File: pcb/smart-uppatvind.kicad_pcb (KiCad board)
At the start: 4 copper layers, 74 x 36 mm, 67 parts, among them J1 PWR, J2 QWIIC, J3 UART_PROG, J4 FAN, Q1 IRLML9301, Q2 MMBT3904, Q3 MMBT3904, Q4 MMBT3904, Q5 Q_NMOS_GSD, SW1 EN, SW2 MAIN, SW3 BOOT, SW4 FILTER, U1 LDL1117S33R, U2 L7980A, U3 ESP32-C3-WROOM-02, U4 M24C02-WMN

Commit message: Added testpoints
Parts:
- added TP1: VIN, TestPoint:TestPoint_THTPad_1.0x1.0mm_Drill0.5mm, F.Cu at (59.8, 75.1)
- added TP2: +5V, TestPoint:TestPoint_THTPad_1.0x1.0mm_Drill0.5mm, F.Cu at (124.6, 74.1)
- added TP3: VDD, TestPoint:TestPoint_THTPad_1.0x1.0mm_Drill0.5mm, F.Cu at (124.6, 70.7)
- added TP4: LED, TestPoint:TestPoint_Pad_1.0x1.0mm, B.Cu at (57.8, 58.3)
- added TP5: FAN_EN, TestPoint:TestPoint_Pad_1.0x1.0mm, B.Cu at (83.0, 53.5)
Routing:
- net /FAN_EN: track 10.8 -> 14.4 mm, vias 0 -> 1
- net /LED: track 29.2 -> 32.2 mm

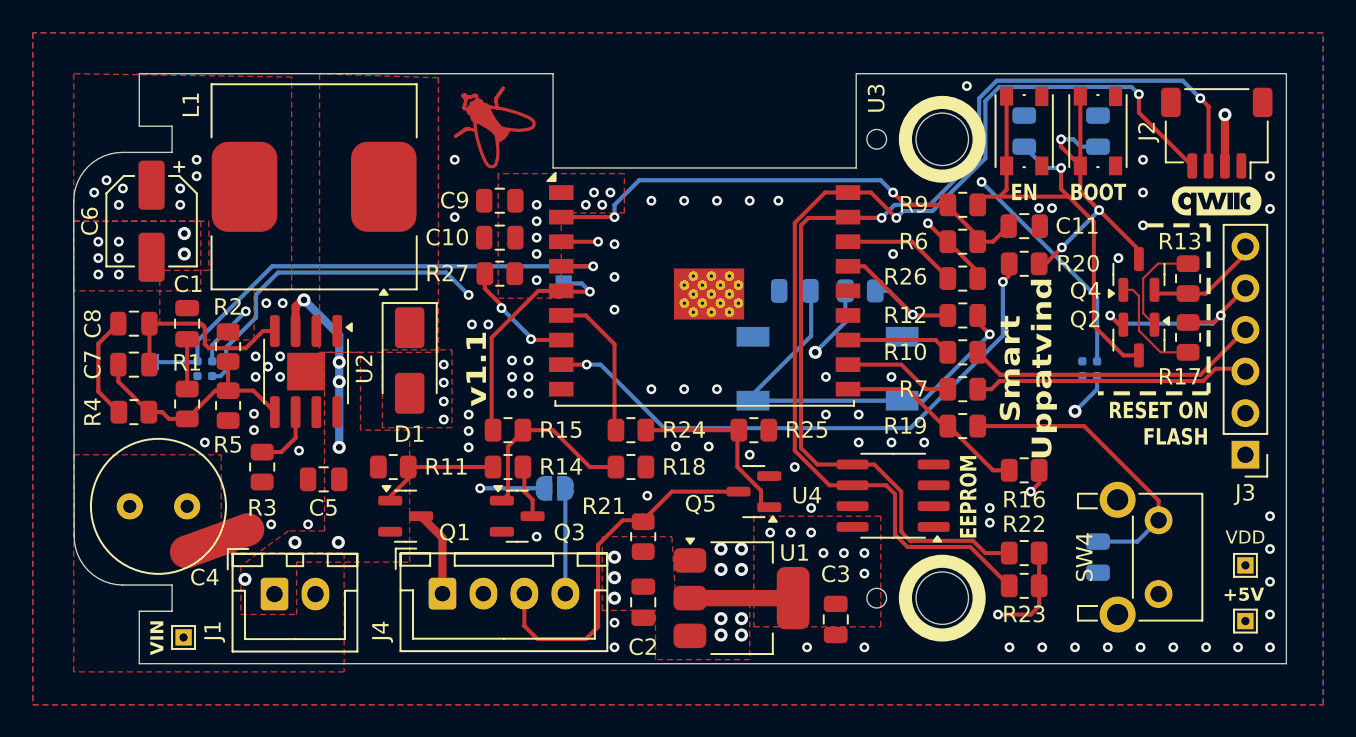
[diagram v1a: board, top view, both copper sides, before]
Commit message: Reannotated components geographically, adjusted designator positions
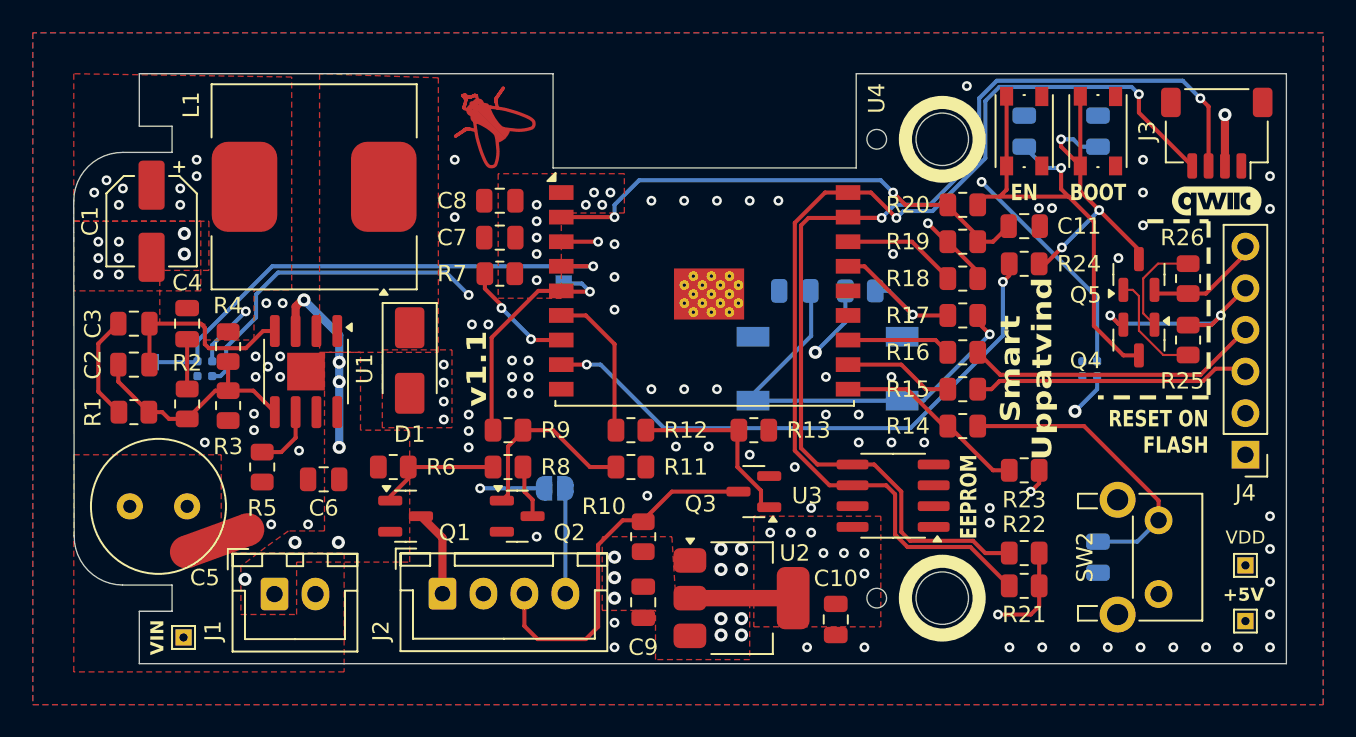
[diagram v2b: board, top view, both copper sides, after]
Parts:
- moved R25 0.16 mm to (121.1, 57.0)
- renumbered C6 to C1, C3 to C10, C14 to C12, C15 to C13, C13 to C14, C12 to C15, C7 to C2, C8 to C3, C1 to C4, C4 to C5, C5 to C6, C10 to C7, C9 to C8, C2 to C9, D3 to D2, D2 to D3, J4 to J2, J2 to J3, J3 to J4, Q3 to Q2, Q5 to Q3, Q2 to Q4, Q4 to Q5, R4 to R1, R21 to R10, R18 to R11, R24 to R12, R25 to R13, R19 to R14, R7 to R15, R10 to R16, R12 to R17, R26 to R18, R6 to R19, R1 to R2, R9 to R20, R23 to R21, R16 to R23, R20 to R24, R17 to R25, R13 to R26, R8 to R27, R5 to R3, R2 to R4, R3 to R5, R11 to R6, R27 to R7, R14 to R8, R15 to R9, SW4 to SW2, SW2 to SW4, TP5 to TP4, TP4 to TP5, U2 to U1, U1 to U2, U4 to U3, U3 to U4

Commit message: Added test point labels to back side, added OSHW symbol
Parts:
- added REF**: OSHW-Logo2_7.3x6mm_SilkScreen, Symbol:OSHW-Logo2_7.3x6mm_SilkScreen, B.Cu at (65.6, 44.7)
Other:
- board text added: "+5V"
- board text added: "VIN"
